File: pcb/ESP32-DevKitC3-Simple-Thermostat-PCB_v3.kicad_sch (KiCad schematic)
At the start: 53 parts, among them J1 PINHD_1x18_Male, J2 Screw_Terminal_9_P3.50mm, J3 DS18B20, J4 3.2 lcd tft, J5 I2C Sensor, J6 LD2410C, J7 PINHD_1x3_Male, K1 G5Q-1A, K2 G5Q-1A, K3 G5Q-1A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

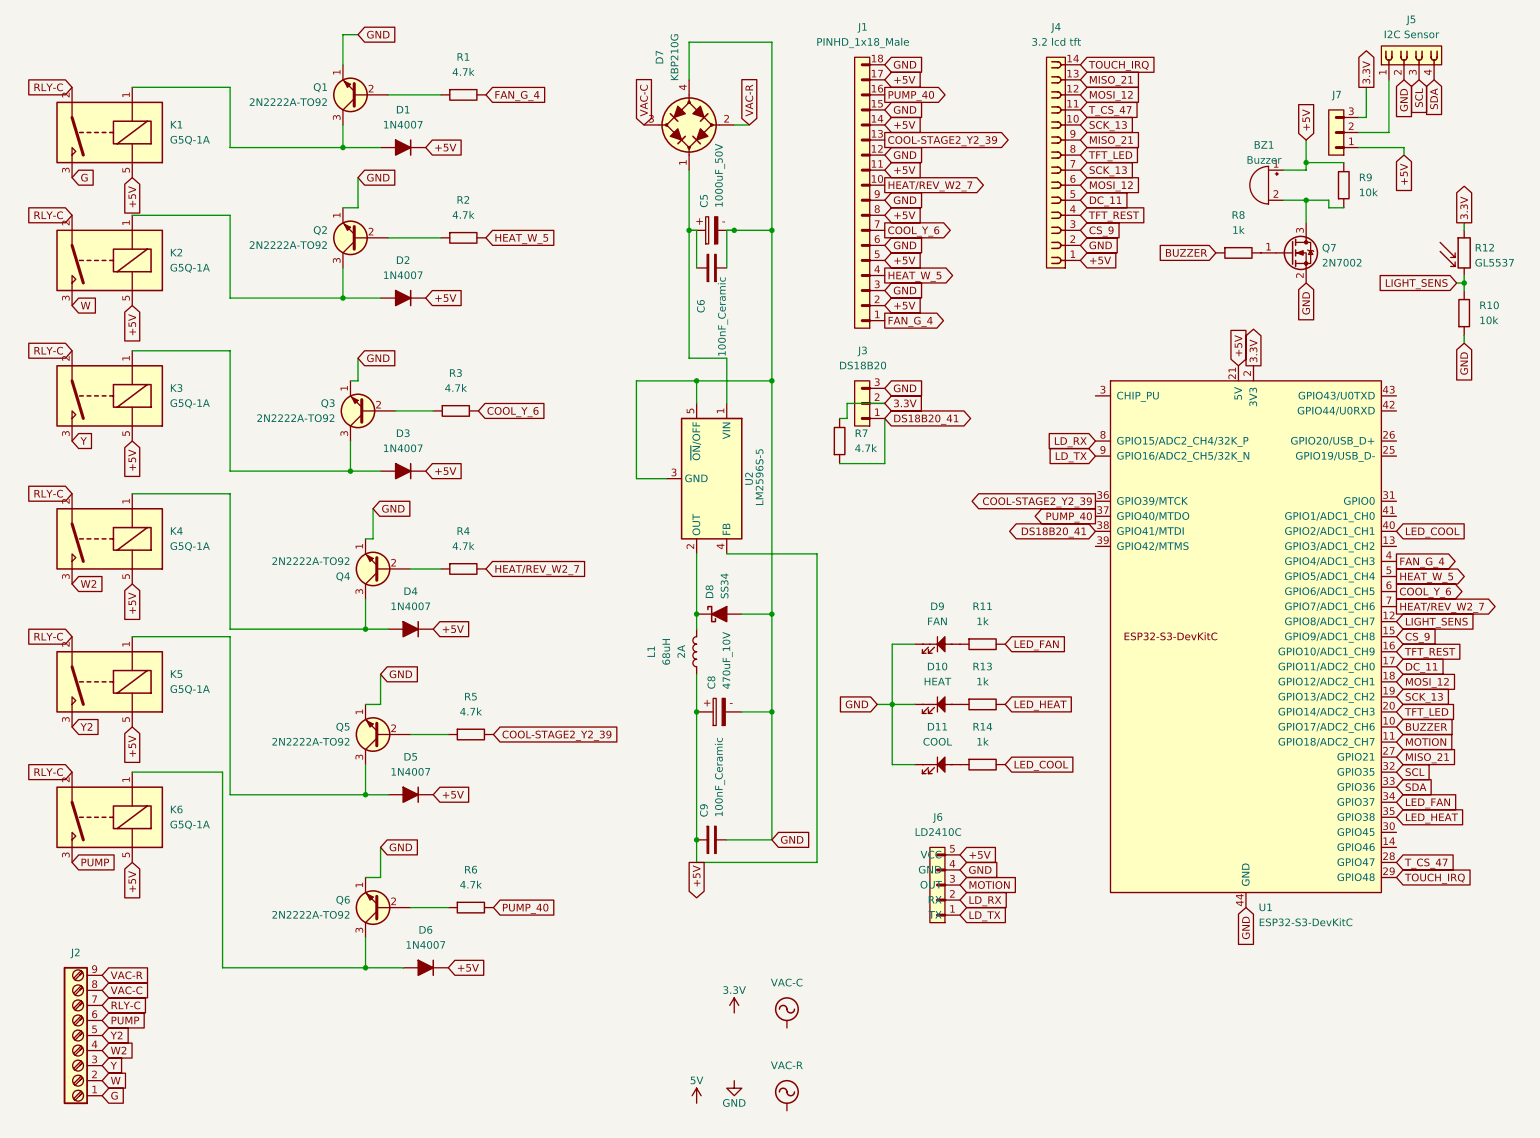
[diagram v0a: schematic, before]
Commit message: PCB v3: replace relays/driver, add 2.8"/4.0" display support headers; firmware fixes
- PCB v3 KiCad design: replaced relay components and relay driver, added
  connector footprints for 2.8" and 4.0" TFT displays alongside existing 3.2"
- New gerbers and JLCPCB production files (BOM, CPL, GERBER zip) for v3
- Remove old v2 gerbers (superseded by v3)
- Firmware builds updated to 20260503 (N8/N16/N32)
- Firmware fixes: debug page JSON overflow, stage 2 heating not escalating,
  right-side sensor text size increased
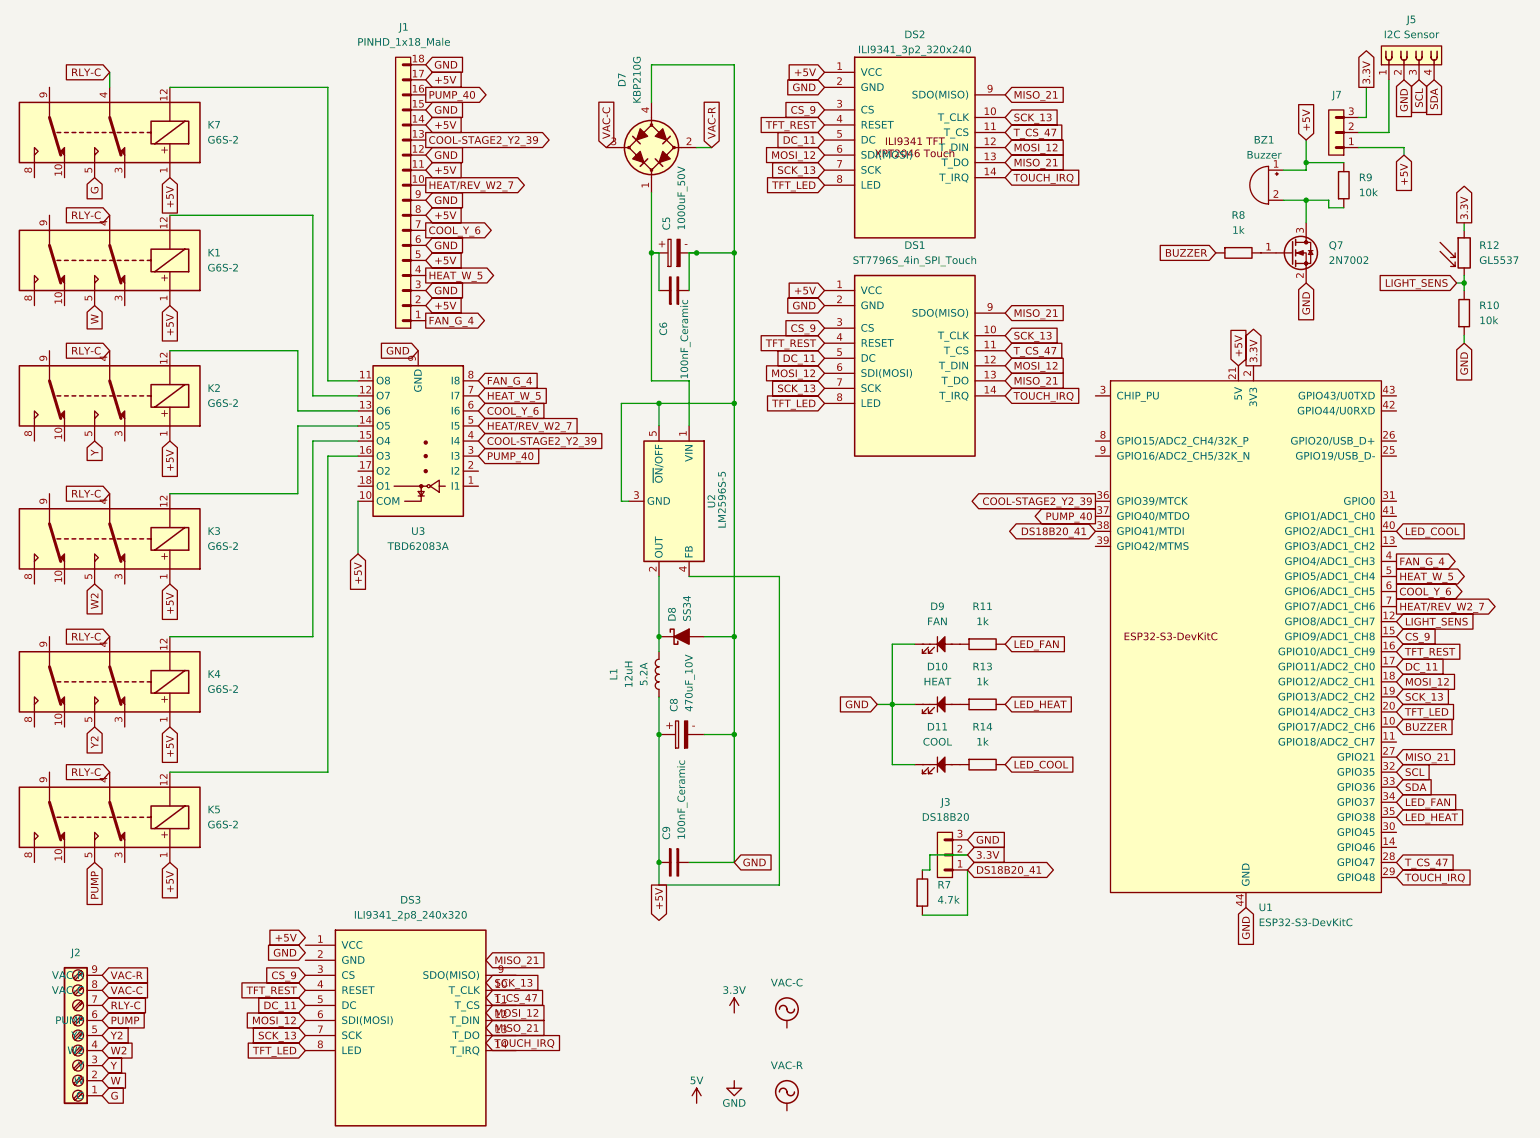
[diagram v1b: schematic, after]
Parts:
- removed D1, D2, D3, D4, D5, D6: 1N4007, PCM_Diode_THT_AKL:D_DO-41_SOD81_P7.62mm_Horizontal, symbol PCM_Diode_AKL:1N4007
- removed J4: 3.2 lcd tft, Connector_PinSocket_2.54mm:PinSocket_1x14_P2.54mm_Vertical, symbol PCM_SL_Pin_Headers:PINHD_1x14_Female
- removed J6: LD2410C, Connector_PinHeader_2.54mm:PinHeader_1x05_P2.54mm_Vertical, symbol PCM_SL_Pin_Headers:PINHD_1x5_Male
- removed K1, K2, K3, K4, K5, K6: G5Q-1A, Relay_THT:Relay_SPST_Omron-G5Q-1A, symbol Relay:G5Q-1A
- removed Q1, Q2, Q3, Q4, Q5, Q6: 2N2222A-TO92, PCM_Package_TO_SOT_THT_AKL:TO-92_Inline_Wide_EBC, symbol PCM_Transistor_BJT_AKL:2N2222A-TO92
- removed R1, R2, R3, R4, R5: 4.7k, Resistor_THT:R_Axial_DIN0207_L6.3mm_D2.5mm_P10.16mm_Horizontal, symbol PCM_SL_Resistors:4.7k
- removed R6: 4.7k, Resistor_THT:R_Axial_DIN0207_L6.3mm_D2.5mm_P10.16mm_Horizontal, symbol PCM_SL_Resistors:Resistor
- added DS1: ST7796S_4in_SPI_Touch, ST7796S_4in_Display:ST7796S_4in_SPI_Touch_Module_14P, symbol ST7796S_4in_Display:ST7796S_4in_SPI_Touch
- added DS2: ILI9341_3p2_320x240, ILI9341_3p2_320x240:ILI9341_3p2_320x240, symbol ILI9341_3p2_320x240:ILI9341_3p2_320x240
- added DS3: ILI9341_2p8_240x320, ILI9341_2p8_240x320:ILI9341_2p8_240x320, symbol ILI9341_2p8_240x320:ILI9341_2p8_240x320
- added K1, K2, K3, K4, K5, K7: G6S-2, Relay_THT:Relay_DPDT_Omron_G6S-2, symbol Relay:G6S-2
- added U3: TBD62083A, footprints:DW18, symbol Transistor_Array:ULN2803A
- BZ1: LCSC (none) -> C76871
- C5: LCSC (none) -> C445418
- C6, C9: LCSC (none) -> C1517817
- C8: LCSC (none) -> C3274796
- D10: LCSC (none) -> C5990731
- D11: LCSC (none) -> C17304835
- D7: LCSC (none) -> C244333
- D8: LCSC (none) -> C908239
- D9: LCSC (none) -> C17340814
- J1: LCSC (none) -> C27985197
- J2: LCSC (none) -> C6373199
- J3, J7: LCSC (none) -> C2932698
- L1: Display 68uH -> 12uH; Display 2 2A -> 5.2A; LCSC (none) -> C2041353
- R10, R9: LCSC (none) -> C119347
- R11, R13, R14, R8: LCSC (none) -> C119324
- R12: LCSC (none) -> C125628
- R7: LCSC (none) -> C119339
- U2: LCSC (none) -> C347445
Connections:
- net +5V: now also DS1.1 (VCC), DS2.1 (VCC), K1.1, K2.1, K3.1, K4.1, K5.1, K7.1, U3.10 (COM)
- net COOL-STAGE2_Y2_39: now also U3.4 (I4)
- net COOL_Y_6: now also U3.6 (I6)
- net CS_9: now also DS1.3 (CS), DS2.3 (CS), DS3.3 (CS)
- net DC_11: now also DS1.5 (DC), DS2.5 (DC), DS3.5 (DC)
- net FAN_G_4: now also U3.8 (I8)
- net G: now also K7.5
- net GND: now also DS1.2 (GND), DS2.2 (GND), U3.9 (GND)
- net HEAT_W_5: now also U3.7 (I7)
- net HEAT/REV_W2_7: now also U3.5 (I5)
- net MISO_21: now also DS1.13 (T_DO), DS1.9 (SDO(MISO)), DS2.13 (T_DO), DS2.9 (SDO(MISO))
- net MOSI_12: now also DS1.12 (T_DIN), DS1.6 (SDI(MOSI)), DS2.12 (T_DIN), DS2.6 (SDI(MOSI)), DS3.6 (SDI(MOSI))
- net PUMP: now also K5.5
- net PUMP_40: now also U3.3 (I3)
- net RLY-C: now also K1.4, K2.4, K3.4, K4.4, K5.4, K7.4
- net SCK_13: now also DS1.10 (T_CLK), DS1.7 (SCK), DS2.10 (T_CLK), DS2.7 (SCK), DS3.7 (SCK)
- net TFT_LED: now also DS1.8 (LED), DS2.8 (LED), DS3.8 (LED)
- net TFT_REST: now also DS1.4 (RESET), DS2.4 (RESET), DS3.4 (RESET)
- net TOUCH_IRQ: now also DS1.14 (T_IRQ), DS2.14 (T_IRQ)
- net T_CS_47: now also DS1.11 (T_CS), DS2.11 (T_CS)
- net W: now also K1.5
- net W2: now also K3.5
- net Y: now also K2.5
- net Y2: now also K4.5
- net LD_RX: no longer names the net of U1.8 (GPIO15/ADC2_CH4/32K_P)
- net LD_TX: no longer names the net of U1.9 (GPIO16/ADC2_CH5/32K_N)
- net MOTION: no longer names the net of U1.11 (GPIO18/ADC2_CH7)
- new net: K2.12, U3.13 (O6)
- new net: K7.12, U3.11 (O8)
- new net: K1.12, U3.12 (O7)
- new net: K3.12, U3.14 (O5)
- new net: K4.12, U3.15 (O4)
- new net: K5.12, U3.16 (O3)
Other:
- moved on the sheet: C5, C6, C8, C9, D7, D8, J1, J3, L1, R7, U2
